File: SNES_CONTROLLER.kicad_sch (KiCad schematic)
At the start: 24 parts, among them J2 Screw_Terminal_01x12, J3 Screw_Terminal_01x12, J4 Screw_Terminal_01x05, U1 4021, U2 4021

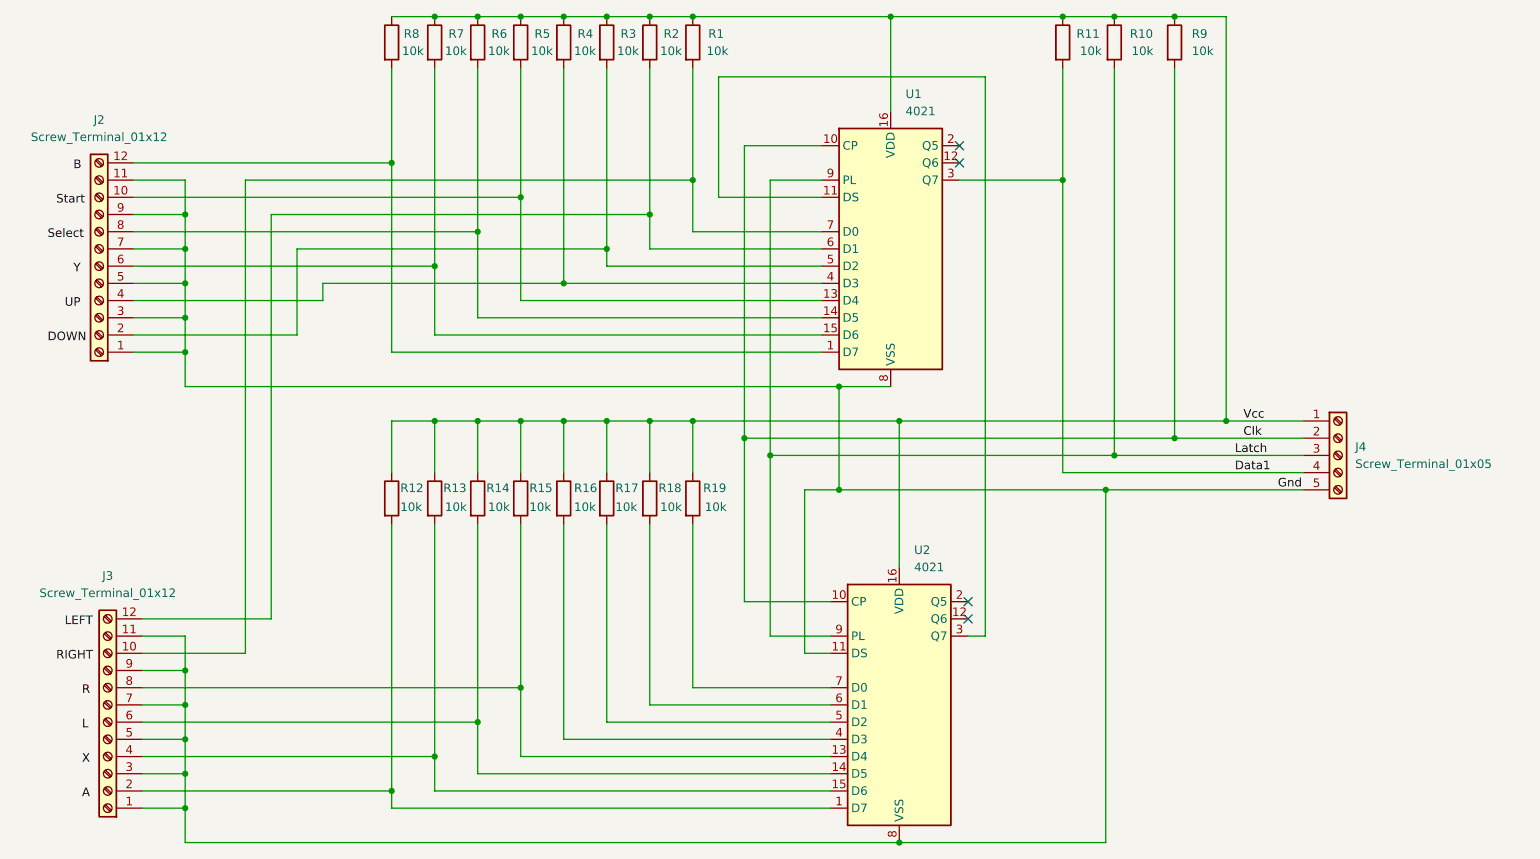
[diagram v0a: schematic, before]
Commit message: Add labels to front silkscreen and mount holes
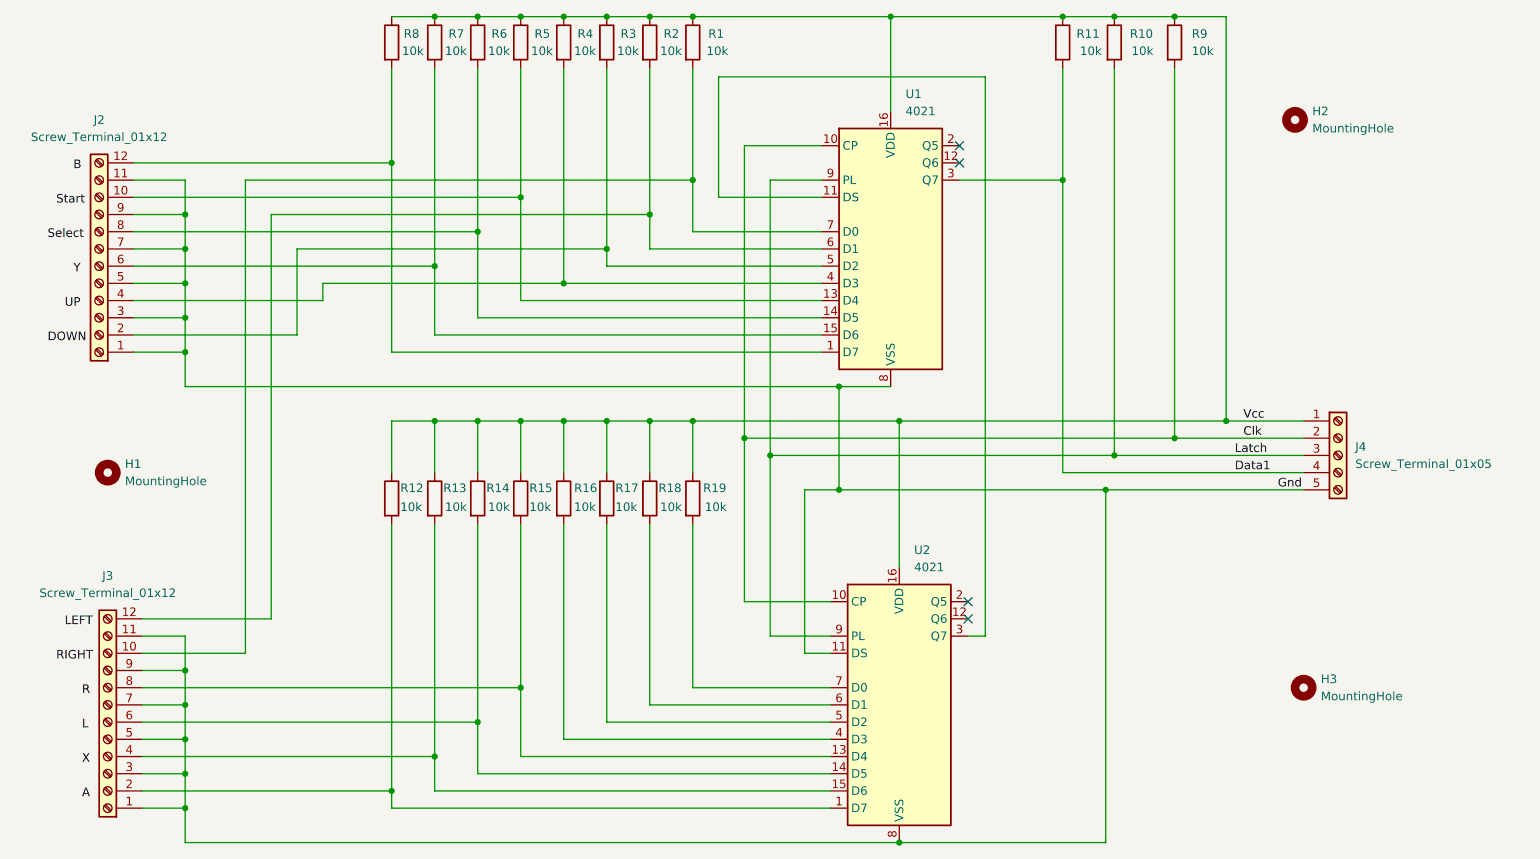
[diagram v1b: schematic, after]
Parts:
- added H1, H2, H3: MountingHole, MountingHole:MountingHole_3.2mm_M3, symbol Mechanical:MountingHole
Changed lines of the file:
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@@
 	(label "A"
 		(at 30.48 156.21 0)
+		(fields_autoplaced yes)
 		(effects
 			(font
@@
 	(label "DOWN"
 		(at 25.4 88.9 0)
+		(fields_autoplaced yes)
 		(effects
 			(font
@@
 	(label "Select"
 		(at 25.4 73.66 0)
+		(fields_autoplaced yes)
 		(effects
 			(font
@@
 	(label "R"
 		(at 30.48 140.97 0)
+		(fields_autoplaced yes)
 		(effects
 			(font
@@
 	(label "UP"
 		(at 27.94 83.82 0)
+		(fields_autoplaced yes)
 		(effects
 			(font
@@
 	(label "Latch"
 		(at 200.66 105.41 0)
+		(fields_autoplaced yes)
 		(effects
 			(font
@@
 	(label "Y"
 		(at 29.21 78.74 0)
+		(fields_autoplaced yes)
 		(effects
 			(font
@@
 	(label "LEFT"
 		(at 27.94 130.81 0)
+		(fields_autoplaced yes)
 		(effects
 			(font
@@
 	(label "Clk"
 		(at 201.93 102.87 0)
+		(fields_autoplaced yes)
 		(effects
 			(font
@@
 	(label "Data1"
 		(at 200.66 107.95 0)
+		(fields_autoplaced yes)
 		(effects
 			(font
@@
 	(label "L"
 		(at 30.48 146.05 0)
+		(fields_autoplaced yes)
 		(effects
 			(font
@@
 	(label "Vcc"
 		(at 201.93 100.33 0)
+		(fields_autoplaced yes)
 		(effects
 			(font
@@
 	(label "X"
 		(at 30.48 151.13 0)
+		(fields_autoplaced yes)
 		(effects
 			(font
@@
 	(label "RIGHT"
 		(at 26.67 135.89 0)
+		(fields_autoplaced yes)
 		(effects
 			(font
@@
 	(label "Gnd"
 		(at 207.01 110.49 0)
+		(fields_autoplaced yes)
 		(effects
 			(font
@@
 	(label "Start"
 		(at 26.67 68.58 0)
+		(fields_autoplaced yes)
 		(effects
 			(font
@@
 	(label "B"
 		(at 29.21 63.5 0)
+		(fields_autoplaced yes)
 		(effects
 			(font
@@
 	)
 	(symbol
+		(lib_id "Mechanical:MountingHole")
+		(at 209.55 55.88 0)
+		(unit 1)
+		(exclude_from_sim yes)
+		(in_bom no)
+		(on_board yes)
+		(dnp no)
+		(fields_autoplaced yes)
+		(property "Reference" "H2"
+			(at 212.09 54.6099 0)
+			(effects
+				(font
+					(size 1.27 1.27)
+				)
+				(justify left)
+			)
+		)
+		(property "Value" "MountingHole"
+			(at 212.09 57.1499 0)
+			(effects
+				(font
+					(size 1.27 1.27)
+				)
+				(justify left)
+			)
+		)
+		(property "Footprint" "MountingHole:MountingHole_3.2mm_M3"
+			(at 209.55 55.88 0)
+			(effects
+				(font
+					(size 1.27 1.27)
+				)
+				(hide yes)
+			)
+		)
+		(property "Datasheet" "~"
+			(at 209.55 55.88 0)
+			(effects
+				(font
+					(size 1.27 1.27)
+				)
+				(hide yes)
+			)
+		)
+		(property "Description" "Mounting Hole without connection"
+			(at 209.55 55.88 0)
+			(effects
+				(font
+					(size 1.27 1.27)
+				)
+				(hide yes)
+			)
+		)
+		(instances
+			(project ""
+				(path "/719592b0-85a8-4eb6-8d13-f447981f3475"
+					(reference "H2")
+					(unit 1)
+				)
+			)
+		)
+	)
+	(symbol
 		(lib_id "Device:R")
 		(at 82.55 44.45 0)
@@
 	)
 	(symbol
+		(lib_id "Mechanical:MountingHole")
+		(at 210.82 139.7 0)
+		(unit 1)
+		(exclude_from_sim yes)
+		(in_bom no)
+		(on_board yes)
+		(dnp no)
+		(fields_autoplaced yes)
+		(property "Reference" "H3"
+			(at 213.36 138.4299 0)
+			(effects
+				(font
+					(size 1.27 1.27)
+				)
+				(justify left)
+			)
+		)
+		(property "Value" "MountingHole"
+			(at 213.36 140.9699 0)
+			(effects
+				(font
+					(size 1.27 1.27)
+				)
+				(justify left)
+			)
+		)
+		(property "Footprint" "MountingHole:MountingHole_3.2mm_M3"
+			(at 210.82 139.7 0)
+			(effects
+				(font
+					(size 1.27 1.27)
+				)
+				(hide yes)
+			)
+		)
+		(property "Datasheet" "~"
+			(at 210.82 139.7 0)
+			(effects
+				(font
+					(size 1.27 1.27)
+				)
+				(hide yes)
+			)
+		)
+		(property "Description" "Mounting Hole without connection"
+			(at 210.82 139.7 0)
+			(effects
+				(font
+					(size 1.27 1.27)
+				)
+				(hide yes)
+			)
+		)
+		(instances
+			(project ""
+				(path "/719592b0-85a8-4eb6-8d13-f447981f3475"
+					(reference "H3")
+					(unit 1)
+				)
+			)
+		)
+	)
+	(symbol
 		(lib_id "4xxx:4021")
 		(at 151.13 142.24 0)
@@
 					(unit 1)
 				)
+			)
+		)
+	)
+	(symbol
+		(lib_id "Mechanical:MountingHole")
+		(at 34.29 107.95 0)
+		(unit 1)
+		(exclude_from_sim yes)
+		(in_bom no)
+		(on_board yes)
+		(dnp no)
+		(fields_autoplaced yes)
+		(property "Reference" "H1"
+			(at 36.83 106.6799 0)
+			(effects
+				(font
+					(size 1.27 1.27)
+				)
+				(justify left)
+			)
+		)
+		(property "Value" "MountingHole"
+			(at 36.83 109.2199 0)
+			(effects
+				(font
+					(size 1.27 1.27)
+				)
+				(justify left)
+			)
+		)
+		(property "Footprint" "MountingHole:MountingHole_3.2mm_M3"
+			(at 34.29 107.95 0)
+			(effects
+				(font
+					(size 1.27 1.27)
+				)
+				(hide yes)
+			)
+		)
+		(property "Datasheet" "~"
+			(at 34.29 107.95 0)
+			(effects
+				(font
+					(size 1.27 1.27)
+				)
+				(hide yes)
+			)
+		)
+		(property "Description" "Mounting Hole without connection"
+			(at 34.29 107.95 0)
+			(effects
+				(font
+					(size 1.27 1.27)
+				)
+				(hide yes)
+			)
+		)
+		(instances
+			(project ""
+				(path "/719592b0-85a8-4eb6-8d13-f447981f3475"
+					(reference "H1")
+					(unit 1)
+				)

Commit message: v1.2 - Use M4 mount holes
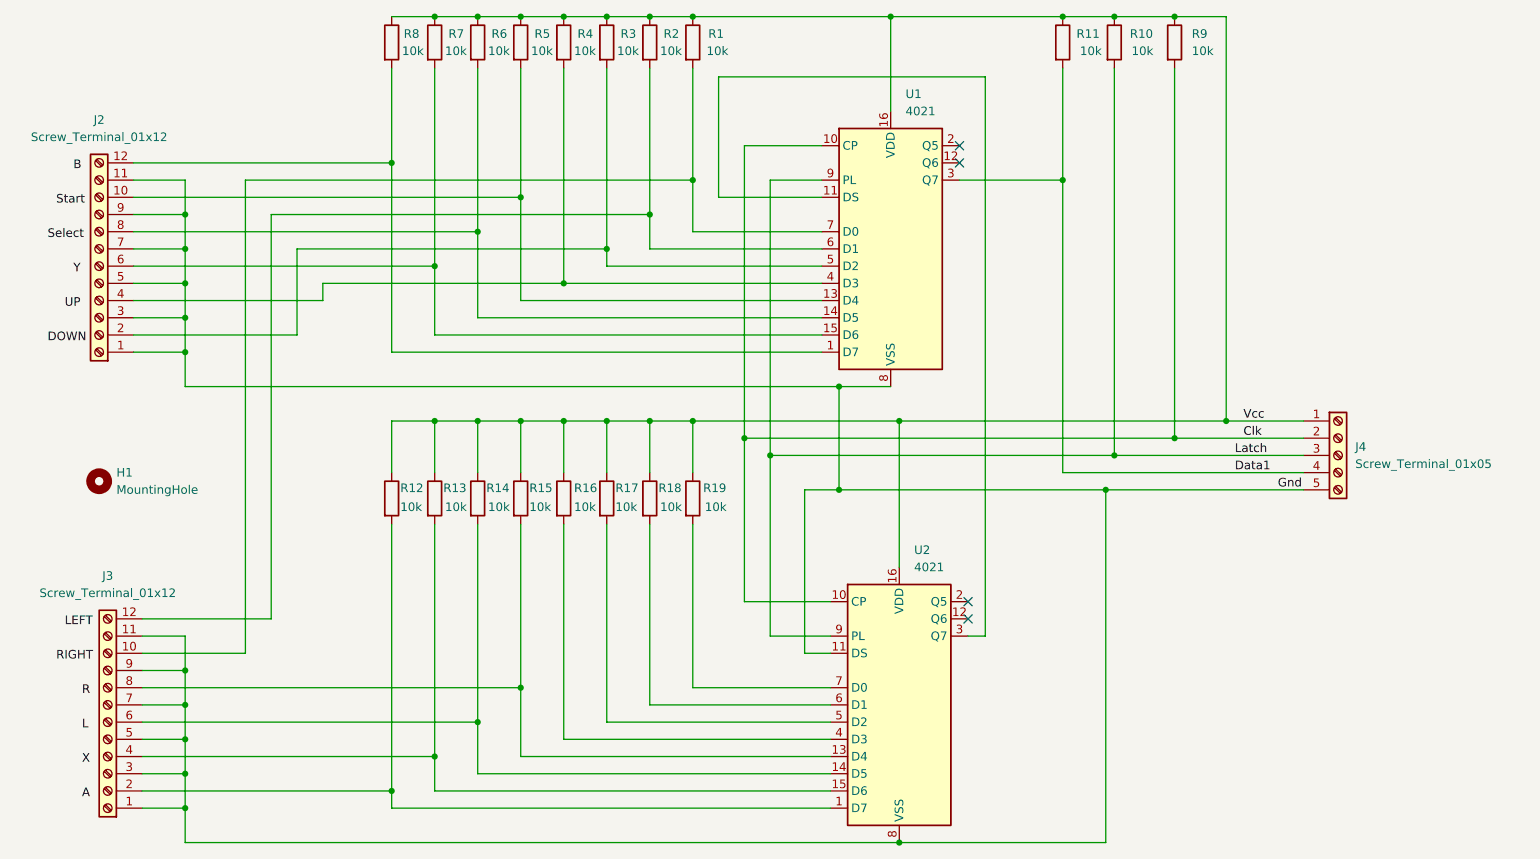
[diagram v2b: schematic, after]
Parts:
- removed H2, H3: MountingHole, MountingHole:MountingHole_3.2mm_M3, symbol Mechanical:MountingHole
- H1: footprint MountingHole:MountingHole_3.2mm_M3 -> MountingHole:MountingHole_4.3mm_M4
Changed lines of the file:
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@@
 (kicad_sch
-	(version 20231120)
+	(version 20250114)
 	(generator "eeschema")
-	(generator_version "8.0")
+	(generator_version "9.0")
 	(paper "A4")
 	(junction
@@
 	(label "A"
 		(at 30.48 156.21 0)
-		(fields_autoplaced yes)
 		(effects
 			(font
@@
 	(label "DOWN"
 		(at 25.4 88.9 0)
-		(fields_autoplaced yes)
 		(effects
 			(font
@@
 	(label "Select"
 		(at 25.4 73.66 0)
-		(fields_autoplaced yes)
 		(effects
 			(font
@@
 	(label "R"
 		(at 30.48 140.97 0)
-		(fields_autoplaced yes)
 		(effects
 			(font
@@
 	(label "UP"
 		(at 27.94 83.82 0)
-		(fields_autoplaced yes)
 		(effects
 			(font
@@
 	(label "Latch"
 		(at 200.66 105.41 0)
-		(fields_autoplaced yes)
 		(effects
 			(font
@@
 	(label "Y"
 		(at 29.21 78.74 0)
-		(fields_autoplaced yes)
 		(effects
 			(font
@@
 	(label "LEFT"
 		(at 27.94 130.81 0)
-		(fields_autoplaced yes)
 		(effects
 			(font
@@
 	(label "Clk"
 		(at 201.93 102.87 0)
-		(fields_autoplaced yes)
 		(effects
 			(font
@@
 	(label "Data1"
 		(at 200.66 107.95 0)
-		(fields_autoplaced yes)
 		(effects
 			(font
@@
 	(label "L"
 		(at 30.48 146.05 0)
-		(fields_autoplaced yes)
 		(effects
 			(font
@@
 	(label "Vcc"
 		(at 201.93 100.33 0)
-		(fields_autoplaced yes)
 		(effects
 			(font
@@
 	(label "X"
 		(at 30.48 151.13 0)
-		(fields_autoplaced yes)
 		(effects
 			(font
@@
 	(label "RIGHT"
 		(at 26.67 135.89 0)
-		(fields_autoplaced yes)
 		(effects
 			(font
@@
 	(label "Gnd"
 		(at 207.01 110.49 0)
-		(fields_autoplaced yes)
 		(effects
 			(font
@@
 	(label "Start"
 		(at 26.67 68.58 0)
-		(fields_autoplaced yes)
 		(effects
 			(font
@@
 	(label "B"
 		(at 29.21 63.5 0)
-		(fields_autoplaced yes)
 		(effects
 			(font
@@
 	)
 	(symbol
-		(lib_id "Mechanical:MountingHole")
-		(at 209.55 55.88 0)
-		(unit 1)
-		(exclude_from_sim yes)
-		(in_bom no)
-		(on_board yes)
-		(dnp no)
-		(fields_autoplaced yes)
-		(property "Reference" "H2"
-			(at 212.09 54.6099 0)
-			(effects
-				(font
-					(size 1.27 1.27)
-				)
-				(justify left)
-			)
-		)
-		(property "Value" "MountingHole"
-			(at 212.09 57.1499 0)
-			(effects
-				(font
-					(size 1.27 1.27)
-				)
-				(justify left)
-			)
-		)
-		(property "Footprint" "MountingHole:MountingHole_3.2mm_M3"
-			(at 209.55 55.88 0)
-			(effects
-				(font
-					(size 1.27 1.27)
-				)
-				(hide yes)
-			)
-		)
-		(property "Datasheet" "~"
-			(at 209.55 55.88 0)
-			(effects
-				(font
-					(size 1.27 1.27)
-				)
-				(hide yes)
-			)
-		)
-		(property "Description" "Mounting Hole without connection"
-			(at 209.55 55.88 0)
-			(effects
-				(font
-					(size 1.27 1.27)
-				)
-				(hide yes)
-			)
-		)
-		(instances
-			(project ""
-				(path "/719592b0-85a8-4eb6-8d13-f447981f3475"
-					(reference "H2")
-					(unit 1)
-				)
-			)
-		)
-	)
-	(symbol
 		(lib_id "Device:R")
 		(at 82.55 44.45 0)
@@
 	)
 	(symbol
-		(lib_id "Mechanical:MountingHole")
-		(at 210.82 139.7 0)
-		(unit 1)
-		(exclude_from_sim yes)
-		(in_bom no)
-		(on_board yes)
-		(dnp no)
-		(fields_autoplaced yes)
-		(property "Reference" "H3"
-			(at 213.36 138.4299 0)
-			(effects
-				(font
-					(size 1.27 1.27)
-				)
-				(justify left)
-			)
-		)
-		(property "Value" "MountingHole"
-			(at 213.36 140.9699 0)
-			(effects
-				(font
-					(size 1.27 1.27)
-				)
-				(justify left)
-			)
-		)
-		(property "Footprint" "MountingHole:MountingHole_3.2mm_M3"
-			(at 210.82 139.7 0)
-			(effects
-				(font
-					(size 1.27 1.27)
-				)
-				(hide yes)
-			)
-		)
-		(property "Datasheet" "~"
-			(at 210.82 139.7 0)
-			(effects
-				(font
-					(size 1.27 1.27)
-				)
-				(hide yes)
-			)
-		)
-		(property "Description" "Mounting Hole without connection"
-			(at 210.82 139.7 0)
-			(effects
-				(font
-					(size 1.27 1.27)
-				)
-				(hide yes)
-			)
-		)
-		(instances
-			(project ""
-				(path "/719592b0-85a8-4eb6-8d13-f447981f3475"
-					(reference "H3")
-					(unit 1)
-				)
-			)
-		)
-	)
-	(symbol
 		(lib_id "4xxx:4021")
 		(at 151.13 142.24 0)
@@
 	)
 	(symbol
-		(lib_id "Device:R")
-		(at 175.26 44.45 0)
+		(lib_id "Mechanical:MountingHole")
+		(at 33.02 109.22 0)
 		(unit 1)
-		(exclude_from_sim no)
-		(in_bom yes)
+		(exclude_from_sim yes)
+		(in_bom no)
 		(on_board yes)
 		(dnp no)
-		(property "Reference" "R11"
-			(at 177.292 43.18 0)
+		(fields_autoplaced yes)
+		(property "Reference" "H1"
+			(at 35.56 107.9499 0)
 			(effects
 				(font
@@
 			)
 		)
-		(property "Value" "10k"
-			(at 177.8 45.7199 0)
+		(property "Value" "MountingHole"
+			(at 35.56 110.4899 0)
 			(effects
 				(font
@@
 			)
 		)
-		(property "Footprint" "Resistor_THT:R_Axial_DIN0207_L6.3mm_D2.5mm_P5.08mm_Vertical"
-			(at 173.482 44.45 90)
+		(property "Footprint" "MountingHole:MountingHole_4.3mm_M4"
+			(at 33.02 109.22 0)
 			(effects
 				(font
@@
 		)
 		(property "Datasheet" "~"
-			(at 175.26 44.45 0)
+			(at 33.02 109.22 0)
 			(effects
 				(font
@@
 			)
 		)
-		(property "Description" "Resistor"
-			(at 175.26 44.45 0)
+		(property "Description" "Mounting Hole without connection"
+			(at 33.02 109.22 0)
 			(effects
 				(font
@@
 			)
 		)
-		(pin "2"
-		)
-		(pin "1"
-		)
 		(instances
-			(project "SNES_CONTROLLER"
+			(project ""
 				(path "/719592b0-85a8-4eb6-8d13-f447981f3475"
-					(reference "R11")
+					(reference "H1")
 					(unit 1)
 				)
@@
 	(symbol
 		(lib_id "Device:R")
-		(at 76.2 44.45 0)
+		(at 175.26 44.45 0)
 		(unit 1)
 		(exclude_from_sim no)
@@
 		(on_board yes)
 		(dnp no)
-		(property "Reference" "R8"
-			(at 77.978 43.18 0)
+		(property "Reference" "R11"
+			(at 177.292 43.18 0)
 			(effects
 				(font
@@
 		)
 		(property "Value" "10k"
-			(at 77.724 45.72 0)
+			(at 177.8 45.7199 0)
 			(effects
 				(font
@@
 		)
 		(property "Footprint" "Resistor_THT:R_Axial_DIN0207_L6.3mm_D2.5mm_P5.08mm_Vertical"
-			(at 74.422 44.45 90)
+			(at 173.482 44.45 90)
 			(effects
 				(font
@@
 		)
 		(property "Datasheet" "~"
-			(at 76.2 44.45 0)
+			(at 175.26 44.45 0)
 			(effects
 				(font
@@
 		)
 		(property "Description" "Resistor"
-			(at 76.2 44.45 0)
+			(at 175.26 44.45 0)
 			(effects
 				(font
@@
 			(project "SNES_CONTROLLER"
 				(path "/719592b0-85a8-4eb6-8d13-f447981f3475"
-					(reference "R8")
+					(reference "R11")
 					(unit 1)
 				)
@@
 	)
 	(symbol
-		(lib_id "Mechanical:MountingHole")
-		(at 34.29 107.95 0)
+		(lib_id "Device:R")
+		(at 76.2 44.45 0)
 		(unit 1)
-		(exclude_from_sim yes)
-		(in_bom no)
+		(exclude_from_sim no)
+		(in_bom yes)
 		(on_board yes)
 		(dnp no)
-		(fields_autoplaced yes)
-		(property "Reference" "H1"
-			(at 36.83 106.6799 0)
+		(property "Reference" "R8"
+			(at 77.978 43.18 0)
 			(effects
 				(font
@@
 			)
 		)
-		(property "Value" "MountingHole"
-			(at 36.83 109.2199 0)
+		(property "Value" "10k"
+			(at 77.724 45.72 0)
 			(effects
 				(font
@@
 			)
 		)
-		(property "Footprint" "MountingHole:MountingHole_3.2mm_M3"
-			(at 34.29 107.95 0)
+		(property "Footprint" "Resistor_THT:R_Axial_DIN0207_L6.3mm_D2.5mm_P5.08mm_Vertical"
+			(at 74.422 44.45 90)
 			(effects
 				(font
@@
 		)
 		(property "Datasheet" "~"
-			(at 34.29 107.95 0)
+			(at 76.2 44.45 0)
 			(effects
 				(font
@@
 			)
 		)
-		(property "Description" "Mounting Hole without connection"
-			(at 34.29 107.95 0)
+		(property "Description" "Resistor"
+			(at 76.2 44.45 0)
 			(effects
 				(font
@@
 			)
 		)
+		(pin "2"
+		)
+		(pin "1"
+		)
 		(instances
-			(project ""
+			(project "SNES_CONTROLLER"
 				(path "/719592b0-85a8-4eb6-8d13-f447981f3475"
-					(reference "H1")
+					(reference "R8")
 					(unit 1)
 				)
@@
 		)
 	)
+	(embedded_fonts no)
 )
